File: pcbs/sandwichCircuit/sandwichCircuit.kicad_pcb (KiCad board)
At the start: 2 copper layers, 76 x 56 mm, 11 parts, among them IC1 3678, J5 Audio Out, U1 ESP32-DevKitC header, U2 CP2104 USB A board

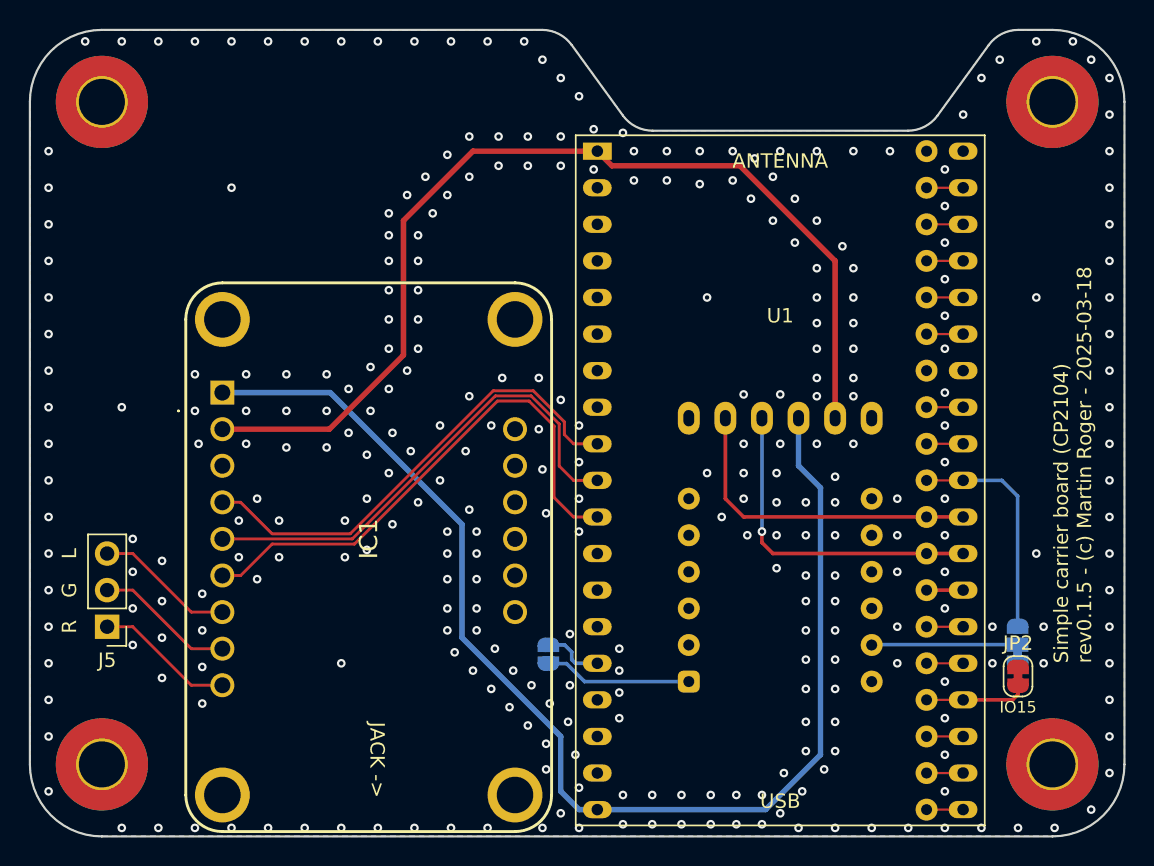
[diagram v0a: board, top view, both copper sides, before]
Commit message: Adding bulk 5V capacitor to SCB
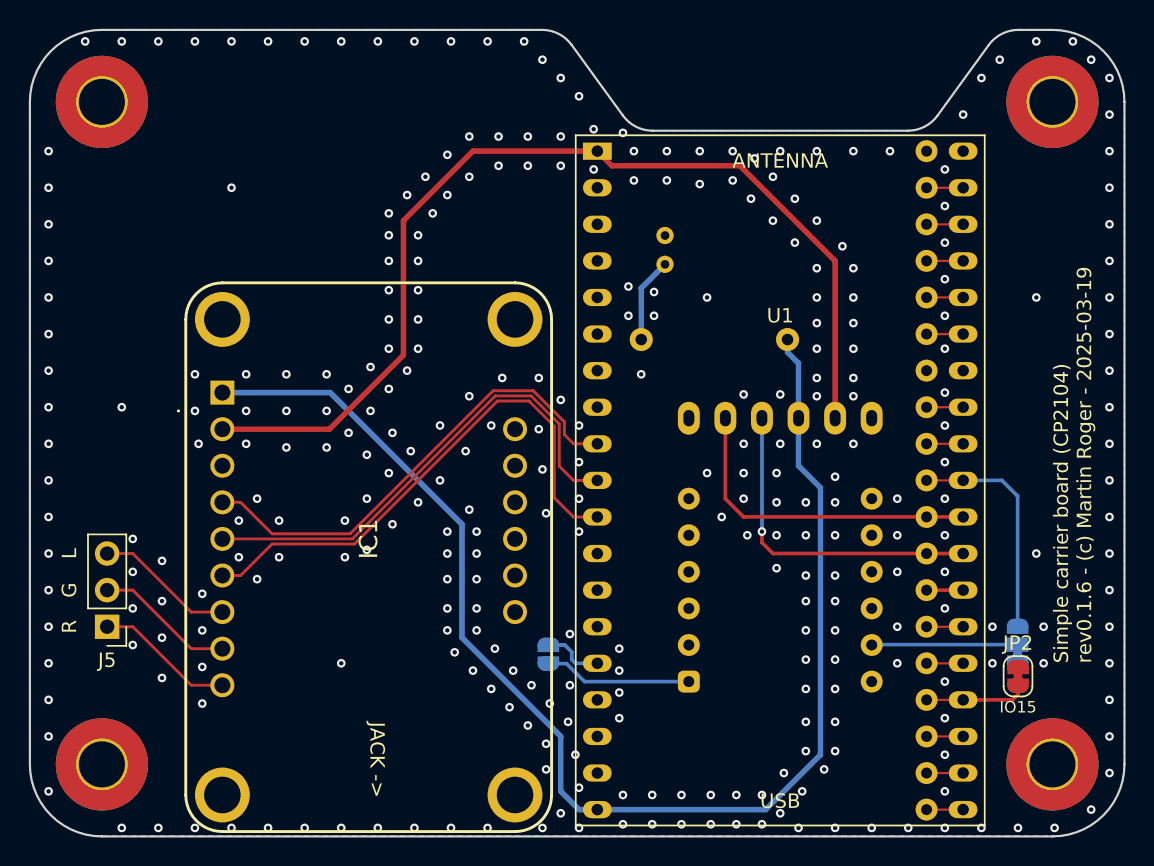
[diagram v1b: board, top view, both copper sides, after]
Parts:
- added C1: 10uF 10V, Capacitor_THT:C_Radial_D5.0mm_H7.0mm_P2.00mm, B.Cu at (157.1, 66.3)
- added R1: 50R, Resistor_THT:R_Axial_DIN0207_L6.3mm_D2.5mm_P10.16mm_Horizontal, B.Cu at (165.6, 71.5)
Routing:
- net Net-(C1-Pad1): track 0.00 -> 5.91 mm
- net +5V: track 85.4 -> 91.2 mm
- net GND: vias 316 -> 321
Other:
- board text added: "10µF 10V"
- board text added: "50Ω"
- board text added: "Fold capacitor ↓↓↓HERE↓↓↓"
